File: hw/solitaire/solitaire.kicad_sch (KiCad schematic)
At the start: 16 parts, among them J1 51441-1093, J3 SBW, J4 BATT_IN, SW1 DEAL, SW2 UNDO, SW3 SKQUCAA010, U1 TPS63900, U2 MSP430FR2355TDBTR

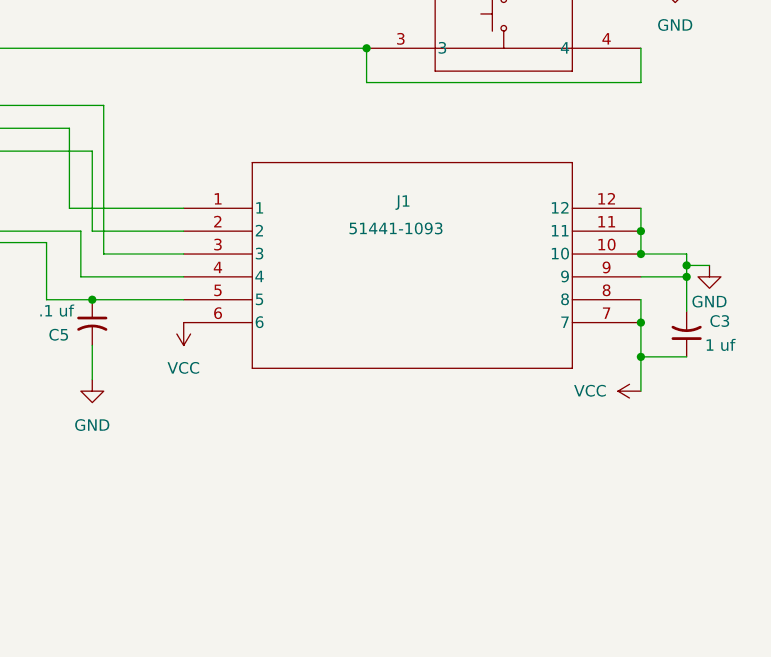
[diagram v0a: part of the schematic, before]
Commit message: Replace obsolete Molex 51441-1093 with GCT FFC2B35-10-T at J1
Molex 51441-1093 (display FPC connector) is EOL/no longer manufactured.
Registers GCT FFC2B35-10-T's symbol/footprint library and swaps J1 over
on both the schematic and PCB, preserving the existing pin-to-signal
mapping (already verified against the Sharp LS013B7DH03's real terminal
numbers) and the existing net assignments.

The new symbol's pin layout differs from the old one (single column vs
two columns of 6), which required adding wiring for pins 6-10 and two
extra pins (11/12, the connector's mechanical/shield pads) that GCT's
stock symbol doesn't expose but the old design tied to GND. PCB footprint
replaced with GCT's real pad geometry at the same position/rotation;
render-verified the cable-entry edge still faces the LCD outline.

Documents the swap and the underlying obsolescence research in
docs/case_design_dimensions.md.

Co-Authored-By: Claude Sonnet 5 <noreply@anthropic.com>
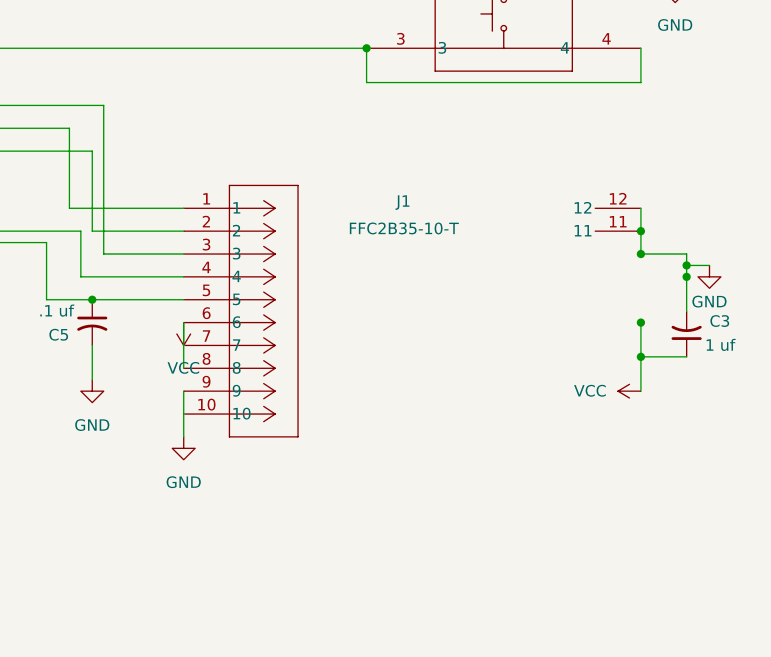
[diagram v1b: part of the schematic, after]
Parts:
- J1: value 51441-1093 -> FFC2B35-10-T; footprint 514411093:CON10_1X10_DRB_51441_MOL -> FFC2B35_10_T:CONN_FFC2B35-10-x_GCT; symbol 514411093:514411093 -> FFC2B35_10_T:FFC2B35-10-T
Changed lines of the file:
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@@
+	(wire
+		(pts
+			(xy 222.25 101.6) (xy 222.25 104.14)
+		)
+		(stroke
+			(width 0)
+			(type default)
+		)
+	)
+	(wire
+		(pts
+			(xy 222.25 104.14) (xy 222.25 106.68)
+		)
+		(stroke
+			(width 0)
+			(type default)
+		)
+	)
+	(wire
+		(pts
+			(xy 222.25 109.22) (xy 222.25 111.76)
+		)
+		(stroke
+			(width 0)
+			(type default)
+		)
+	)
+	(wire
+		(pts
+			(xy 222.25 111.76) (xy 222.25 114.3)
+		)
+		(stroke
+			(width 0)
+			(type default)
+		)
+	)
 	(wire
 		(pts
@@
 		(pts
 			(xy 213.36 77.47) (xy 213.36 93.98)
-		)
-		(stroke
-			(width 0)
-			(type default)
-		)
-	)
-	(wire
-		(pts
-			(xy 273.05 99.06) (xy 273.05 101.6)
 		)
 		(stroke
@@
 	(wire
 		(pts
-			(xy 273.05 96.52) (xy 278.13 96.52)
-		)
-		(stroke
-			(width 0)
-			(type default)
-		)
-	)
-	(wire
-		(pts
 			(xy 276.86 59.69) (xy 276.86 63.5)
 		)
@@
 	(symbol
 		(lib_id "power:GND")
+		(at 222.25 114.3 0)
+		(unit 1)
+		(exclude_from_sim no)
+		(in_bom yes)
+		(on_board yes)
+		(dnp no)
+		(fields_autoplaced yes)
+		(property "Reference" "#PWR019"
+			(at 222.25 120.65 0)
+			(effects
+				(font
+					(size 1.27 1.27)
+				)
+				(hide yes)
+			)
+		)
+		(property "Value" "GND"
+			(at 222.25 119.38 0)
+			(effects
+				(font
+					(size 1.27 1.27)
+				)
+			)
+		)
+		(property "Footprint" ""
+			(at 222.25 114.3 0)
+			(effects
+				(font
+					(size 1.27 1.27)
+				)
+				(hide yes)
+			)
+		)
+		(property "Datasheet" ""
+			(at 222.25 114.3 0)
+			(effects
+				(font
+					(size 1.27 1.27)
+				)
+				(hide yes)
+			)
+		)
+		(property "Description" "Power symbol creates a global label with name \"GND\" , ground"
+			(at 222.25 114.3 0)
+			(effects
+				(font
+					(size 1.27 1.27)
+				)
+				(hide yes)
+			)
+		)
+		(pin "1"
+		)
+		(instances
+			(project ""
+				(path "/37bed383-82de-493d-be12-9430e997c33d"
+					(reference "#PWR019")
+					(unit 1)
+				)
+			)
+		)
+	)
+	(symbol
+		(lib_id "power:GND")
 		(at 193.04 48.26 0)
 		(unit 1)
@@
 	)
 	(symbol
-		(lib_id "514411093:514411093")
+		(lib_id "FFC2B35_10_T:FFC2B35-10-T")
 		(at 222.25 88.9 0)
 		(unit 1)
@@
 			)
 		)
-		(property "Value" "51441-1093"
+		(property "Value" "FFC2B35-10-T"
 			(at 240.538 91.186 0)
 			(effects
@@
 			)
 		)
-		(property "Footprint" "514411093:CON10_1X10_DRB_51441_MOL"
+		(property "Footprint" "FFC2B35_10_T:CONN_FFC2B35-10-x_GCT"
 			(at 222.25 88.9 0)
 			(effects
@@
 			)
 		)
-		(property "Datasheet" "514411093"
+		(property "Datasheet" "FFC2B35-10-T"
 			(at 222.25 88.9 0)
 			(effects
@@
 			)
 		)
-		(property "Description" "Molex 51441-1093, 10-position 0.5mm pitch bottom-contact FPC/FFC connector"
+		(property "Description" "GCT FFC2B35-10-T, 10-position 0.5mm pitch bottom-contact front-flip FPC/FFC connector - replacement for obsolete Molex 51441-1093"
 			(at 222.25 88.9 0)
 			(effects
